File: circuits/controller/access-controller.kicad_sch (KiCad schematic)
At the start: 24 parts, among them J1 RJ45_JK0-0177NL, J10 Conn_02x06_Odd_Even, J11 Terminal_01x04, J12 Terminal_01x03, J13 Terminal_01x03, J14 Terminal_01x03, J15 Terminal_01x04, J17 Screw_Terminal_01x05, J2 Barrel_Jack_OD5.5_ID2.5, J20 Conn_01x01_Female, J21 Conn_01x01_Female, J22 Conn_01x01_Female, J23 Conn_01x01_Female, J3 Terminal_01x04, J4 Terminal_01x03, J5 Terminal_01x03, J6 Terminal_01x03, J7 Terminal_01x04, J9 Screw_Terminal_01x05, U1 MCP23017_SS

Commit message: sent to fab! 0.6
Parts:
- removed J1: RJ45_JK0-0177NL, Open_Automation:RJ45_JK0-0177NL, symbol Open_Automation:RJ45_JK0-0177NL
- removed J11, J15, J3, J7: Terminal_01x04, TerminalBlock_Phoenix:TerminalBlock_Phoenix_MKDS-3-4-5.08_1x04_P5.08mm_Horizontal, symbol Open Automation:Terminal_01x04
- removed J12, J13, J14, J4, J5, J6: Terminal_01x03, TerminalBlock_Phoenix:TerminalBlock_Phoenix_MKDS-3-3-5.08_1x03_P5.08mm_Horizontal, symbol Open_Automation:Terminal_01x03
- removed J17, J9: Screw_Terminal_01x05, TerminalBlock_Phoenix:TerminalBlock_Phoenix_MKDS-3-5-5.08_1x05_P5.08mm_Horizontal, symbol Open Automation:Screw_Terminal_01x05
- removed J2: Barrel_Jack_OD5.5_ID2.5, Open_Automation:BarrelJack_OD5.5_ID2.5, symbol Open_Automation:Barrel_Jack_OD5.5_ID2.5
- removed R1, R2: R_10K_0402, Resistor_SMD:R_0402_1005Metric_Pad0.72x0.64mm_HandSolder, symbol Open_Automation:R_10K_0402
- added C1, C2: C_470uF, Capacitor_SMD:CP_Elec_10x10, symbol open_automation:C_470uF
- added J10, J15, J16, J17, J8, J9: Terminal_01x03, TerminalBlock_Phoenix:TerminalBlock_Phoenix_MKDS-3-3-5.08_1x03_P5.08mm_Horizontal, symbol open_automation:Terminal_01x03
- added J11, J14, J18, J7: Terminal_01x04, TerminalBlock_Phoenix:TerminalBlock_Phoenix_MKDS-3-4-5.08_1x04_P5.08mm_Horizontal, symbol open_automation:Terminal_01x04
- added J12, J19: Screw_Terminal_01x05, TerminalBlock_Phoenix:TerminalBlock_Phoenix_MKDS-3-5-5.08_1x05_P5.08mm_Horizontal, symbol open_automation:Screw_Terminal_01x05
- added J6: Screw_Terminal_01x02, TerminalBlock_Phoenix:TerminalBlock_Phoenix_MKDS-1,5-2-5.08_1x02_P5.08mm_Horizontal, symbol open_automation:Screw_Terminal_01x02
- added J9: Barrel_Jack_Switch, Open_Automation:BarrelJack_OD5.5_ID2.5, symbol open_automation:Barrel_Jack_Switch
- added Q14: Q_MMBT5551, Package_TO_SOT_SMD:SOT-23, symbol Open_Automation:Q_MMBT5551
- added R63: R_100, Resistor_SMD:R_0402_1005Metric_Pad0.72x0.64mm_HandSolder, symbol Open_Automation:R_100
- LS1: value S_YXDZ -> TMB12A05; LCSC (none) -> C96093; Part Number YXDZ -> TMB12A05
- renumbered J20 to J1, J10 to J13, J21 to J2, J22 to J3, J23 to J4
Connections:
- net SPEAKER is gone; now on net 5V: LS1.1
- net EXIT0: now also J8.3 (Pin_3)
- net EXIT1: now also J15.3 (Pin_3)
- net FOB0: now also J10.3 (Pin_3)
- net FOB1: now also J17.3 (Pin_3)
- net GND: now also C1.2, C2.2, J10.2 (Pin_2), J12.2 (Pin_2), J14.2 (Pin_2), J15.2 (Pin_2), J16.2 (Pin_2), J17.2 (Pin_2), J19.2 (Pin_2), J6.2 (Pin_2), J7.2 (Pin_2), J8.2 (Pin_2), J9.2, J9.2 (Pin_2), J9.3, Q14.2 (E); no longer LS1.2
- net KEYPAD0: now also J7.3 (Pin_3)
- net KEYPAD1: now also J14.3 (Pin_3)
- net LOCK0_CLOSE: now also J11.4 (Pin_4)
- net LOCK0_OUT: now also J11.2 (Pin_2)
- net LOCK0_STATE: now also J11.3 (Pin_3)
- net LOCK1_CLOSE: now also J18.4 (Pin_4)
- net LOCK1_OUT: now also J18.2 (Pin_2)
- net LOCK1_STATE: now also J18.3 (Pin_3)
- net MOTION0: now also J9.3 (Pin_3)
- net MOTION1: now also J16.3 (Pin_3)
- net POWER: now also C1.1, C2.1, J11.1 (Pin_1), J18.1 (Pin_1), J6.1 (Pin_1), J9.1
- net PUSH0: now also J12.5 (Pin_5), J7.4 (Pin_4)
- net PUSH1: now also J14.4 (Pin_4), J19.5 (Pin_5)
- net REG_POWER: now also J10.1 (Pin_1), J12.1 (Pin_1), J14.1 (Pin_1), J15.1 (Pin_1), J16.1 (Pin_1), J17.1 (Pin_1), J19.1 (Pin_1), J7.1 (Pin_1), J8.1 (Pin_1), J9.1 (Pin_1)
- net WG0_DATA0: now also J12.3 (Pin_3)
- net WG0_DATA1: now also J12.4 (Pin_4)
- net WG1_DATA0: now also J19.3 (Pin_3)
- net WG1_DATA1: now also J19.4 (Pin_4)
- new net: LS1.2, Q14.3 (C)
- new net: Q14.1 (B), R63.2
- new net BUZZER: R63.1
- no-connect marks 6 -> 0
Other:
- removed sheet PoE
- removed sheet USB
- sheet Ethernet ports: added CS, MISO, MOSI, POWER, SCLK; removed EMAC_CLK_OUT, EMAC_RXD0, EMAC_RXD1, EMAC_RX_CRS_DV, EMAC_TXD0, EMAC_TXD1, EMAC_TX_EN, LL+, LL-, MDC, MDCT1, MDCT2, MDIO, PHY_PWR, RD+, RD-, RL+, RL-, TD+, TD-
- sheet Microcontroller ports: added 5V, I2C_CLK, I2C_DATA, IO10, IO11, IO3, IO6, IO7, IO8, IO9; removed ESP_EN, IO13, IO14, IO15, IO16, IO17, IO18, IO19, IO21, IO22, IO23, IO25, IO26, IO27, IO32, IO33, IO34, IO35, PROG, RXD, TXD
- moved on the sheet: J13, LS1, U1

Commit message: added polarity to speaker, added lcsc part for header
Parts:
- J13: LCSC (none) -> C2884015; Part Number (none) -> X6521WVS-2x06H-C60D74
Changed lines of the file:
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@@
+      (effects (font (size 1.27 1.27)) hide)
+    )
+    (property "Part Number" "X6521WVS-2x06H-C60D74" (at 121.031 60.452 0)
+      (effects (font (size 1.27 1.27)) hide)
+    )
+    (property "LCSC" "C2884015" (at 121.031 60.452 0)
       (effects (font (size 1.27 1.27)) hide)
     )

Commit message: testing radar
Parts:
- added D4 (x19): White, LED_SMD:LED_0603_1608Metric_Pad1.05x0.95mm_HandSolder, symbol open_automation:LED-0603-W
- added R11 (x19): 10K, Resistor_SMD:R_0402_1005Metric_Pad0.72x0.64mm_HandSolder, symbol Open_Automation:R_10K_0402
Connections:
- net EXIT0: now also D4.2 (A)
- net EXIT1: now also D4.2 (A)
- net FOB0: now also D4.2 (A)
- net FOB1: now also D4.2 (A)
- net GND: now also R11.1, R11.1, R11.1, R11.1, R11.1, R11.1, R11.1, R11.1, R11.1, R11.1, R11.1, R11.1, R11.1, R11.1, R11.1, R11.1, R11.1
- net KEYPAD0: now also D4.2 (A)
- net KEYPAD1: now also D4.2 (A)
- net LOCK0_CLOSE: now also D4.2 (A)
- net LOCK0_OUT: now also R11.1
- net LOCK0_STATE: now also D4.2 (A)
- net LOCK1_CLOSE: now also D4.2 (A)
- net LOCK1_OUT: now also R11.1
- net LOCK1_STATE: now also D4.2 (A)
- net MOTION0: now also D4.2 (A)
- net MOTION1: now also D4.2 (A)
- net POWER: now also D4.2 (A), D4.2 (A), D4.2 (A)
- net WG0_DATA0: now also D4.2 (A)
- net WG0_DATA1: now also D4.2 (A)
- net WG1_DATA0: now also D4.2 (A)
- net WG1_DATA1: now also D4.2 (A)
- new net: D4.1 (K), R11.2 (x19)
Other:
- moved on the sheet: J10, J11, J12, J13, J14, J15, J16, J17, J18, J19, J7, J8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

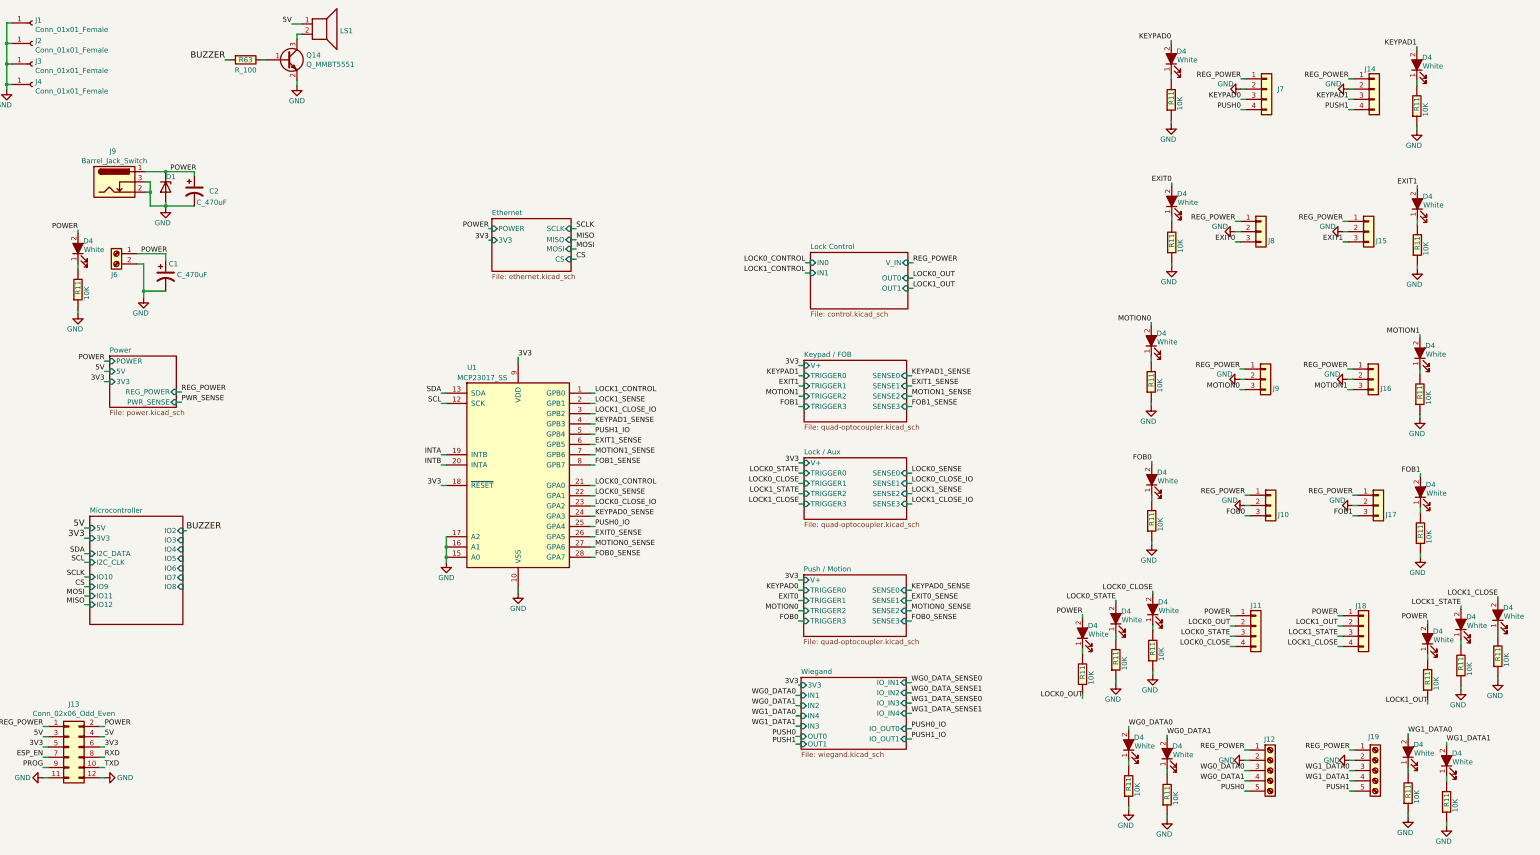
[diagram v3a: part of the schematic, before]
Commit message: Remove obsolete access controller lock file and multiple outdated backup zip files. Enhance automation service with improved logging, including a shutdown handler and better memory management for log persistence. Introduce new API routes for Wiegand state management and update related services for improved functionality and error handling.
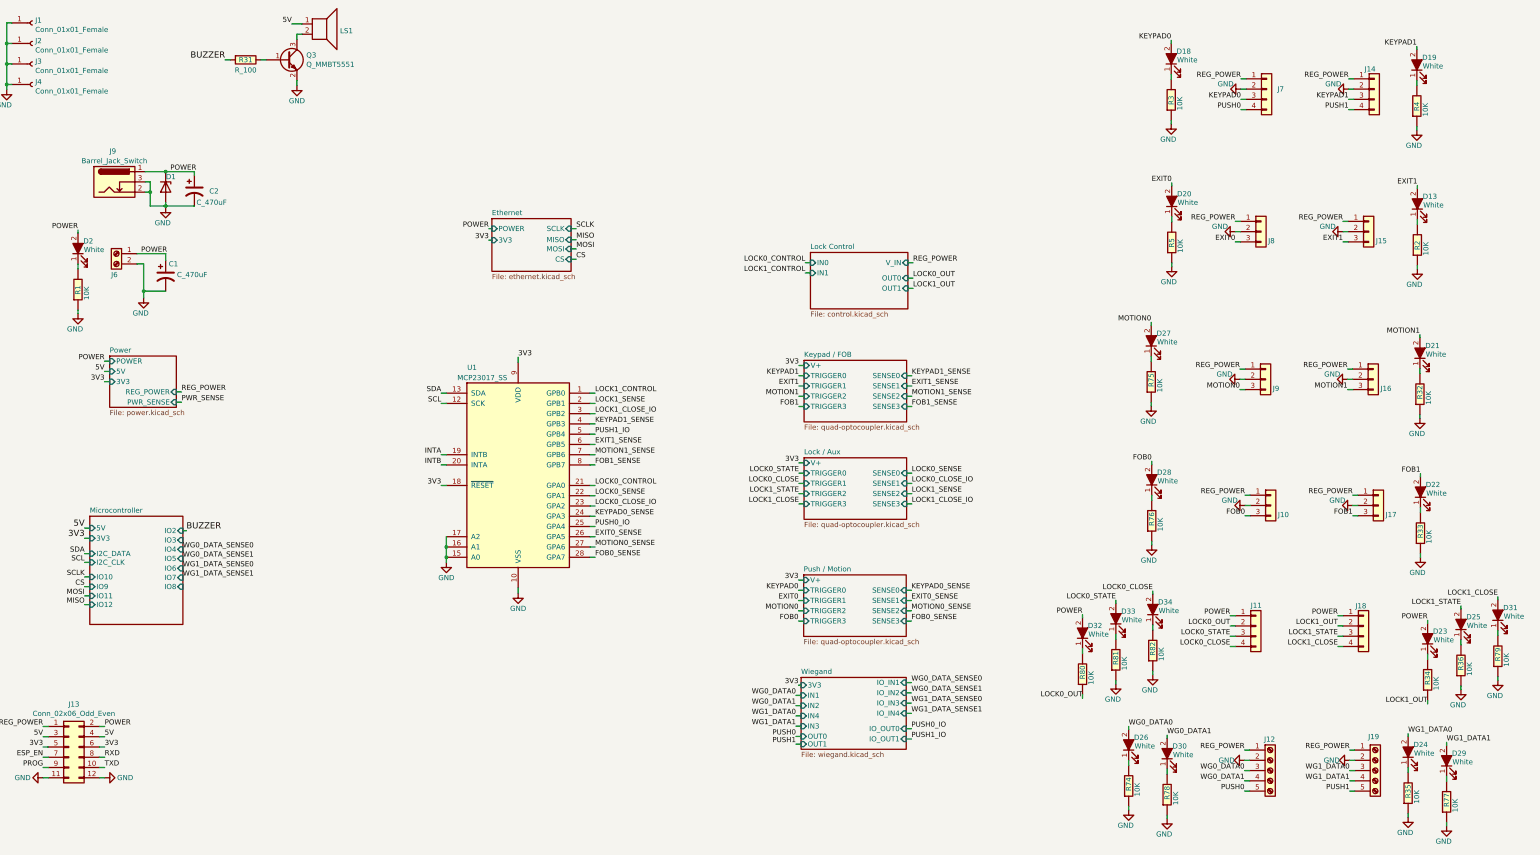
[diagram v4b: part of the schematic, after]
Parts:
- renumbered D4 to D13, D4 to D18, D4 to D19, D4 to D2, D4 to D20, D4 to D21, D4 to D22, D4 to D23, D4 to D24, D4 to D25, D4 to D26, D4 to D27, D4 to D28, D4 to D29, D4 to D30, D4 to D31, D4 to D32, D4 to D33, D4 to D34, Q14 to Q3, R11 to R1, R11 to R2, R11 to R3, R63 to R31, R11 to R32, R11 to R33, R11 to R34, R11 to R35, R11 to R36, R11 to R4, R11 to R5, R11 to R74, R11 to R75, R11 to R76, R11 to R77, R11 to R78, R11 to R79, R11 to R80, R11 to R81, R11 to R82

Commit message: order from fab
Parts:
- added J22: RF_MODULE, Library:RXB6_RF_MODULE, symbol Connector_Generic:Conn_01x09
- added Q4: Q_MMBT5551, Package_TO_SOT_SMD:SOT-23, symbol Open_Automation:Q_MMBT5551
- added R83, R84: 10K, Resistor_SMD:R_0402_1005Metric_Pad0.72x0.64mm_HandSolder, symbol Open_Automation:R_10K_0402
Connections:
- net 3V3: now also R84.1
- net 5V: now also J22.4 (Pin_4), J22.5 (Pin_5)
- net GND: now also J22.1 (Pin_1), J22.6 (Pin_6), J22.7 (Pin_7), Q4.2 (E)
- new net: Q4.1 (B), R83.1
- new net ANTENNA: J22.8 (Pin_8), J22.9 (Pin_9)
- new net DATA: J22.2 (Pin_2), R83.2
- new net DATA_IO: Q4.3 (C), R84.2
- no-connect marks 0 -> 1
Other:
- sheet Microcontroller ports: added IO15; removed none
